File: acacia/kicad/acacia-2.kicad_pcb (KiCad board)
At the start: 2 copper layers, 274 x 158 mm, 127 parts, among them J1 USB4500-03-0-A, SW1 A, SW10 C, SW11 R, SW12 F, SW13 V, SW14 T, SW15 G, SW16 Back, SW17 Gui, SW18 Ctl, SW19 Alt, SW2 Z, SW20 Sft, SW21 Fwd, SW22 AltGr, SW23 L2, SW24 L1, SW25 Ctl, SW26 U, SW27 J, SW28 M, SW29 N, SW3 Tab, SW30 Enter, SW31 I, SW32 K, SW33 Comm, SW34 O, SW35 L, SW36 Dot, SW38 P, SW39 Semi, SW4 B, SW40 Slsh, SW41 H, SW42 Y, SW43 QMK, SW48 Q, SW49 RESET, SW5 W, SW6 S, SW7 X, SW8 E, SW9 D, U1 USBLC6-2SC6, U2 ATmega32U2-A, Y1 16MHz

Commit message: wip
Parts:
- removed D20, D25, D30, D41: D, Diode_SMD:D_0805_2012Metric_Pad1.15x1.40mm_HandSolder
- removed SW20: Sft, mech-kbd:MX-Hotswap-1U
- removed SW25: Ctl, mech-kbd:MX-Hotswap-1U
- removed SW29: N, mech-kbd:MX-Hotswap-1U
- removed SW30: Enter, mech-kbd:MX-Hotswap-1U
- removed SW43: QMK, Button_Switch_SMD:SW_SPST_EVQQ2
- removed TP5: C2, TestPoint:TestPoint_Pad_1.0x1.0mm
- removed TP6: C4, TestPoint:TestPoint_Pad_1.0x1.0mm
- removed TP7: C5, TestPoint:TestPoint_Pad_1.0x1.0mm
- added C10: 4µ7, Capacitor_SMD:CP_Elec_8x6.9, F.Cu at (110.4, 123.0)
- added C7: 47µ, Capacitor_SMD:CP_Elec_8x6.9, F.Cu at (110.4, 113.1)
- added C9: 100n, Capacitor_SMD:C_0805_2012Metric_Pad1.18x1.45mm_HandSolder, F.Cu at (95.3, 139.0)
- added FB3: 120@100M, Inductor_SMD:L_0805_2012Metric_Pad1.15x1.40mm_HandSolder, F.Cu at (90.6, 139.0)
- added FB4: 120@100M, Inductor_SMD:L_0805_2012Metric_Pad1.15x1.40mm_HandSolder, F.Cu at (90.6, 142.0)
- added U3: ATmega32U4-A, Package_QFP:TQFP-44_10x10mm_P0.8mm, F.Cu at (192.4, 123.8)
- D1, D10, D11, D12, D13, D14, D15, D16, D17, D18, D19, D2, D21, D22, D23, D24, D26, D27, D28, D29, D3, D31, D32, D33, D34, D35, D36, D37, D38, D39, D4, D40, D48, D5, D6, D7, D8, D9: moved to F.Cu
- SW12: value F -> T
- SW14: value T -> L1
- SW15: value G -> Prv
- SW16: value Back -> G
- SW17: value Gui -> B
- SW18: value Ctl -> Sft
- SW19: value Alt -> L2
- SW21: value Fwd -> H
- SW22: value AltGr -> K
- SW23: value L2 -> Spc
- SW24: value L1 -> Esc
- SW27: value J -> N
- SW32: value K -> E
- SW33: value Comm -> Com
- SW39: value Semi -> Y
- SW4: value B -> Nxt
- SW40: value Slsh -> J
- SW41: value H -> Del
- SW42: value Y -> Ent
- SW8: value E -> F
- TP1: value GND -> GNDD
- TP3: value D0 -> 5V; footprint TestPoint:TestPoint_Pad_1.0x1.0mm -> TestPoint:TestPoint_Pad_1.5x1.5mm; moved to F.Cu
- TP4: value D1 -> 3V3; footprint TestPoint:TestPoint_Pad_1.0x1.0mm -> TestPoint:TestPoint_Pad_1.5x1.5mm; moved to F.Cu
- U2: value ATmega32U2-A -> NCP1117; footprint Package_QFP:TQFP-32_7x7mm_P0.8mm -> Package_TO_SOT_SMD:TO-252-2; moved to F.Cu
- Y1: value 16MHz -> 8MHz
- moved SW21 217.2 mm to (37.7, 73.8), turned to 0 degrees
- moved SW42 205.3 mm to (78.1, 94.0), turned to 0 degrees
- moved SW40 199.0 mm to (78.1, 53.6), turned to 0 degrees
- moved SW36 194.7 mm to (57.9, 134.4), turned to 0 degrees
- moved SW39 194.6 mm to (78.1, 33.4), turned to 0 degrees
- moved H5 191.8 mm to (92.2, 119.7)
- moved SW38 190.6 mm to (78.1, 13.2), turned to 0 degrees
- moved SW22 188.3 mm to (37.7, 94.0), turned to 0 degrees
- moved SW35 187.8 mm to (57.9, 114.2), turned to 0 degrees
- moved SW28 181.0 mm to (57.9, 13.2), turned to 0 degrees
- moved SW34 181.0 mm to (57.9, 94.0), turned to 0 degrees
- moved SW27 173.3 mm to (37.7, 134.4), turned to 0 degrees
- moved SW33 170.6 mm to (57.9, 73.8), turned to 0 degrees
- moved SW26 164.8 mm to (37.7, 114.2), turned to 0 degrees
- moved SW32 163.5 mm to (57.9, 53.6), turned to 0 degrees
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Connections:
- C1 pad 1: GND -> GNDD
- C2 pad 1: Net-(C2-Pad1) -> GND
- C3 pad 1: Net-(C3-Pad1) -> Net-(U3-XTAL1)
- C3 pad 2: GND -> GNDD
- C4 pad 1: Net-(C4-Pad1) -> Net-(U3-XTAL2)
- C4 pad 2: GND -> GNDD
- C5 pad 1: Net-(C5-Pad1) -> Net-(U3-UCAP)
- C5 pad 2: GND -> GNDD
- C6 pad 2: GND -> GNDD
- C8 pad 1: +5V -> +3V3
- C8 pad 2: GND -> GNDD
- D15 pad 1: R4 -> R3
- D4 pad 1: R4 -> R3
- F1 pad 1: Net-(C1-Pad2) -> /VBUS
- F1 pad 2: +5V -> Net-(C1-Pad2)
- FB1 pad 1: GND -> GNDD
- FB1 pad 2: Net-(C2-Pad1) -> GND
- FB2 pad 1: /VBUS -> Net-(C1-Pad2)
- FB2 pad 2: Net-(C1-Pad2) -> +5V
- R1 pad 1: Net-(C2-Pad1) -> GND
- R4 pad 1: +5V -> +3V3
- R4 pad 2: Net-(C7-Pad1) -> Net-(R4-Pad2)
- R5 pad 1: Net-(C7-Pad1) -> Net-(R4-Pad2)
- R5 pad 2: ~{RESET} -> Net-(U3-~{RESET})
- R6 pad 1: Net-(R6-Pad1) -> Net-(U3-~{HWB}/PE2)
- R6 pad 2: GND -> GNDD
- SW15 pad 2: C3 -> C2
- SW4 pad 2: C0 -> C7
- SW49 pad 1: ~{RESET} -> Net-(R4-Pad2)
- SW49 pad 2: GND -> GNDD
- TP1 pad 1: GND -> GNDD
- TP3 pad 1: Net-(TP3-Pad1) -> Net-(C7-Pad1)
- TP4 pad 1: Net-(TP4-Pad1) -> +3V3
- U2 pad 1: Net-(C3-Pad1) -> GNDD
- U2 pad 2: Net-(C4-Pad1) -> +3V3
- U2 pad 3: GND -> +5V
- Y1 pad 1: Net-(C3-Pad1) -> Net-(U3-XTAL1)
- Y1 pad 2: Net-(C4-Pad1) -> Net-(U3-XTAL2)
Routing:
- net R4: track 382.6 -> 52.9 mm, vias 5 -> 0
- net R0: track 417.2 -> 107.1 mm, vias 10 -> 0
- net +3V3: track 0.00 -> 294.5 mm, vias 0 -> 1
- net (no net): track 0.00 -> 272.5 mm
- net R1: track 351.2 -> 595.2 mm, vias 13 -> 4
- net C0: track 217.2 -> 115.2 mm, vias 3 -> 1
- net C3: track 119.7 -> 45.2 mm, vias 3 -> 0
- net Net-(D26-A): track 4.04 -> 74.5 mm, vias 0 -> 2
- net Net-(D29-A): track 6.50 -> 71.5 mm
- net C7: track 162.9 -> 216.3 mm, vias 2 -> 0
- net C5: track 166.6 -> 215.2 mm
- net Net-(D20-Pad2): track 25.0 -> 0.00 mm
- net Net-(D22-A): track 10.8 -> 35.2 mm
- net GNDD: track 0.00 -> 17.8 mm, vias 0 -> 2
- net Net-(U3-XTAL1): track 0.00 -> 15.9 mm
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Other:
- board text added: "2023 jpsecher v2"
- board text removed: "2022 jpsecher"

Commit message: WIP: v2 board
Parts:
- removed C10: 4µ7, Capacitor_SMD:CP_Elec_8x6.9
- removed the C7 at (110.4, 113.1)
- removed the C7 at (144.5, 121.0)
- removed C9: 100n, Capacitor_SMD:C_0805_2012Metric_Pad1.18x1.45mm_HandSolder
- removed D48: D, Diode_SMD:D_0805_2012Metric_Pad1.15x1.40mm_HandSolder
- removed FB3, FB4: 120@100M, Inductor_SMD:L_0805_2012Metric_Pad1.15x1.40mm_HandSolder
- removed SW40: J, mech-kbd:MX-Hotswap-1U
- removed SW41: Del, mech-kbd:MX-Hotswap-1U
- removed SW42: Ent, mech-kbd:MX-Hotswap-1U
- removed SW48: Q, mech-kbd:MX-Hotswap-1U
- removed SW49: RESET, Button_Switch_SMD:SW_SPST_EVQQ2
- removed TP3: 5V, TestPoint:TestPoint_Pad_1.5x1.5mm
- removed TP4: 3V3, TestPoint:TestPoint_Pad_1.5x1.5mm
- removed U3: ATmega32U4-A, Package_QFP:TQFP-44_10x10mm_P0.8mm
- added C7: 4µ7, Capacitor_SMD:C_0805_2012Metric_Pad1.18x1.45mm_HandSolder, B.Cu at (125.8, 192.8)
- added D20: D, Diode_SMD:D_0805_2012Metric_Pad1.15x1.40mm_HandSolder, B.Cu at (116.2, 162.5)
- added D25: D, Diode_SMD:D_0805_2012Metric_Pad1.15x1.40mm_HandSolder, B.Cu at (111.4, 153.4)
- added D30: D, Diode_SMD:D_0805_2012Metric_Pad1.15x1.40mm_HandSolder, B.Cu at (111.4, 168.6)
- added D41: SK6805, LED_SMD:LED_SK6805_PLCC4_2.4x2.7mm_P1.3mm, B.Cu at (170.7, 146.6)
- added D42: SK6805, LED_SMD:LED_SK6805_PLCC4_2.4x2.7mm_P1.3mm, B.Cu at (177.9, 138.5)
- added D43: SK6805, LED_SMD:LED_SK6805_PLCC4_2.4x2.7mm_P1.3mm, B.Cu at (186.7, 138.6)
- added J2: USB4500-03-0-A, mech-kbd:USB4500030A, B.Cu at (158.9, 49.4)
- added SW20: Y, mech-kbd:MX-Hotswap-1U, F.Cu at (263.6, 67.8)
- added SW25: V, mech-kbd:MX-Hotswap-1U, F.Cu at (105.5, 90.2)
- added SW29: Com, mech-kbd:MX-Hotswap-1U, F.Cu at (226.1, 76.2)
- added SW30: Dot, mech-kbd:MX-Hotswap-1U, F.Cu at (247.0, 80.2)
- added SW37: Del, mech-kbd:MX-Hotswap-1U, F.Cu at (210.5, 111.1)
- C1: value 4µ7 -> 1µ; footprint Capacitor_SMD:C_0805_2012Metric_Pad1.18x1.45mm_HandSolder -> Capacitor_SMD:C_1206_3216Metric_Pad1.33x1.80mm_HandSolder
- C2: value 22p -> 1µ
- C6: footprint Capacitor_SMD:C_1206_3216Metric_Pad1.33x1.80mm_HandSolder -> Capacitor_SMD:C_0805_2012Metric_Pad1.18x1.45mm_HandSolder
- C8: value 1µ -> 22p
- D1, D10, D11, D12, D13, D14, D15, D16, D17, D18, D19, D2, D21, D22, D23, D24, D26, D27, D28, D29, D3, D31, D32, D33, D34, D35, D36, D37, D38, D4, D5, D6, D7, D8, D9, H1, H10, H2, H3, H4, H5, H6, H7, H8, H9: moved to B.Cu
- D39, D40: value D -> SK6805; footprint Diode_SMD:D_0805_2012Metric_Pad1.15x1.40mm_HandSolder -> LED_SMD:LED_SK6805_PLCC4_2.4x2.7mm_P1.3mm; moved to B.Cu
- J1: value USB4500-03-0-A -> Trackpad; footprint mech-kbd:USB4500030A -> Connector:FanPinHeader_1x04_P2.54mm_Vertical
- R1: value 1M -> 10k
- R3: value 22 -> 10k
- R4: value 10k -> 5k1
- R5: value 22 -> 5k1
- R6: value 10k -> 22
- R7: value 5k1 -> 22
- R8: value 5k1 -> 1M
- SW1: value A -> Q
- SW10: value C -> P
- SW11: value R -> A
- SW12: value T -> S
- SW13: value V -> D
- SW14: value L1 -> T
- SW15: value Prv -> B
- SW16: value G -> K
- SW17: value B -> N
- SW18: value Sft -> E; footprint mech-kbd:MX-Hotswap-1.5U -> mech-kbd:MX-Hotswap-1U
- SW19: value L2 -> L; footprint mech-kbd:MX-Hotswap-1.25U -> mech-kbd:MX-Hotswap-1U
- SW2: value Z -> W
- SW21: value H -> RESET; footprint mech-kbd:MX-Hotswap-1U -> Button_Switch_SMD:SW_SPST_EVQQ2; moved to B.Cu
- SW22: value K -> Z
- SW23: value Spc -> X; footprint mech-kbd:MX-Hotswap-1.5U -> mech-kbd:MX-Hotswap-1U
- SW24: value Esc -> C; footprint mech-kbd:MX-Hotswap-1.25U -> mech-kbd:MX-Hotswap-1U
- SW26: value U -> Sft; footprint mech-kbd:MX-Hotswap-1U -> mech-kbd:MX-Hotswap-1.5U
- SW27: value N -> Spc; footprint mech-kbd:MX-Hotswap-1U -> mech-kbd:MX-Hotswap-1.5U
- SW3: value Tab -> F
- SW31: value I -> J
- SW32: value E -> Tab; footprint mech-kbd:MX-Hotswap-1U -> mech-kbd:MX-Hotswap-1.5U
- SW33: value Com -> Prv; footprint mech-kbd:MX-Hotswap-1U -> mech-kbd:MX-Hotswap-1.5U
- SW34: value O -> L1
- SW35: value L -> L2; footprint mech-kbd:MX-Hotswap-1U -> mech-kbd:MX-Hotswap-1.5U
- SW36: value Dot -> Esc; footprint mech-kbd:MX-Hotswap-1U -> mech-kbd:MX-Hotswap-1.5U
- SW38: value P -> Nxt; footprint mech-kbd:MX-Hotswap-1U -> mech-kbd:MX-Hotswap-1.5U
- SW39: value Y -> Ent; footprint mech-kbd:MX-Hotswap-1U -> mech-kbd:MX-Hotswap-1.5U
- SW4: value Nxt -> R
- SW5: value W -> G
- SW6: value S -> H
- SW7: value X -> U
- SW8: value F -> I
- SW9: value D -> O
- TP1: value GNDD -> 5V
- TP2: value 5V -> GNDD
- U1: value USBLC6-2SC6 -> ATmega32U4-A; footprint Package_TO_SOT_SMD:SOT-23-6 -> Package_QFP:TQFP-44_10x10mm_P0.8mm
- U2: value NCP1117 -> USBLC6-2SC6; footprint Package_TO_SOT_SMD:TO-252-2 -> Package_TO_SOT_SMD:SOT-23-6; moved to B.Cu
- Y1: value 8MHz -> 16MHz
- moved SW10 241.1 mm to (258.6, 49.5), turned to 15 degrees
- moved SW9 219.9 mm to (237.2, 43.4), turned to 15 degrees
- moved SW7 217.9 mm to (199.6, 53.5), turned to 15 degrees
- moved SW31 217.1 mm to (268.5, 86.2), turned to 15 degrees
- moved SW39 206.0 mm to (282.0, 62.9), turned to -75 degrees
- moved SW8 200.4 mm to (216.2, 39.5), turned to 15 degrees
- moved SW6 192.3 mm to (183.9, 67.6), turned to 15 degrees
- moved H1 184.0 mm to (272.5, 51.1), turned to 180 degrees
- moved SW38 176.5 mm to (232.2, 99.2), turned to -75 degrees
- moved SW28 170.0 mm to (209.5, 90.1), turned to 15 degrees
- moved SW17 167.9 mm to (204.6, 71.8), turned to 15 degrees
- moved SW16 159.9 mm to (188.7, 86.0), turned to 15 degrees
- moved H2 158.4 mm to (250.5, 92.2), turned to 180 degrees
- moved SW27 155.3 mm to (191.9, 116.2), turned to -75 degrees
- moved H3 152.6 mm to (227.5, 33.2), turned to 180 degrees
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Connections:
- C1 pad 1: GNDD -> +5V
- C1 pad 2: Net-(C1-Pad2) -> GNDD
- C2 pad 1: GND -> +5V
- C2 pad 2: GNDPWR -> GNDD
- C3 pad 1: Net-(U3-XTAL1) -> Net-(U1-XTAL1)
- C4 pad 1: Net-(U3-XTAL2) -> Net-(U1-XTAL2)
- C5 pad 1: Net-(U3-UCAP) -> Net-(U1-UCAP)
- C8 pad 1: +3V3 -> GND
- C8 pad 2: GNDD -> GNDPWR
- D1 pad 1: R1 -> R0
- D10 pad 1: R2 -> R0
- D11 pad 1: R0 -> R1
- D13 pad 1: R2 -> R1
- D14 pad 1: R3 -> R1
- D15 pad 1: R3 -> R1
- D16 pad 1: R0 -> R1
- D18 pad 1: R2 -> R1
- D19 pad 1: R3 -> R1
- D2 pad 1: R2 -> R0
- D21 pad 1: R0 -> R2
- D22 pad 1: R1 -> R2
- D24 pad 1: R3 -> R2
- D26 pad 1: R0 -> R2
- D27 pad 1: R1 -> R2
- D29 pad 1: R3 -> R2
- D3 pad 1: R3 -> R0
- D31 pad 1: R0 -> R3
- D32 pad 1: R1 -> R3
- D33 pad 1: R2 -> R3
- D34 pad 1: R0 -> R3
- D35 pad 1: R1 -> R3
- D36 pad 1: R2 -> R3
- D37 pad 1: R0 -> R3
- D38 pad 1: R1 -> R3
- D39 pad 1: R2 -> Net-(D39-DOUT)
- D39 pad 2: Net-(D39-A) -> GNDD
- D4 pad 1: R3 -> R0
- D40 pad 1: R3 -> Net-(D40-DOUT)
- D40 pad 2: Net-(D40-A) -> GNDD
- D6 pad 1: R1 -> R0
- D7 pad 1: R2 -> R0
- D9 pad 1: R1 -> R0
- F1 pad 2: Net-(C1-Pad2) -> Net-(C7-Pad2)
- FB1 pad 1: GNDD -> Net-(C7-Pad2)
- FB1 pad 2: GND -> +5V
- FB2 pad 1: Net-(C1-Pad2) -> GNDD
- FB2 pad 2: +5V -> GND
- R1 pad 1: GND -> +5V
- R1 pad 2: GNDPWR -> Net-(R1-Pad2)
- R2 pad 1: /DDD- -> Net-(R1-Pad2)
- R2 pad 2: DDDD- -> Net-(U1-~{RESET})
- R3 pad 1: /DDD+ -> Net-(U1-~{HWB}/PE2)
- R3 pad 2: DDDD+ -> GNDD
- R4 pad 1: +3V3 -> Net-(J2-CC1)
- R4 pad 2: Net-(R4-Pad2) -> GND
- R5 pad 1: Net-(R4-Pad2) -> Net-(J2-CC2)
- R5 pad 2: Net-(U3-~{RESET}) -> GND
- R6 pad 1: Net-(U3-~{HWB}/PE2) -> /DDD-
- R6 pad 2: GNDD -> DDDD-
- R7 pad 1: Net-(J1-CC1) -> /DDD+
- R7 pad 2: GND -> DDDD+
- R8 pad 1: Net-(J1-CC2) -> GND
- R8 pad 2: GND -> GNDPWR
- SW10 pad 2: C2 -> C9
- SW11 pad 2: C3 -> C0
- SW12 pad 2: C3 -> C1
- SW13 pad 2: C3 -> C2
- SW15 pad 2: C2 -> C4
- SW16 pad 2: C4 -> C5
- SW17 pad 2: C4 -> C6
- SW18 pad 2: C4 -> C7
- SW19 pad 2: C4 -> C8
- SW2 pad 2: C0 -> C1
- SW21 pad 1: Net-(D21-A) -> Net-(R1-Pad2)
- SW21 pad 2: C5 -> GNDD
- SW22 pad 1: Net-(D22-A) -> Net-(D21-A)
- SW22 pad 2: C5 -> C0
- SW23 pad 1: Net-(D23-A) -> Net-(D22-A)
- SW23 pad 2: C5 -> C1
- SW24 pad 1: Net-(D24-A) -> Net-(D23-A)
- SW24 pad 2: C5 -> C2
- SW26 pad 1: Net-(D26-A) -> Net-(D25-A)
- SW26 pad 2: C6 -> C4
- SW27 pad 1: Net-(D27-A) -> Net-(D26-A)
- SW27 pad 2: C6 -> C5
- SW28 pad 1: Net-(D28-A) -> Net-(D27-A)
- SW3 pad 2: C0 -> C2
- SW31 pad 1: Net-(D31-A) -> Net-(D30-A)
- SW31 pad 2: C7 -> C9
- SW32 pad 1: Net-(D32-A) -> Net-(D31-A)
- SW32 pad 2: C7 -> C0
- SW33 pad 1: Net-(D33-A) -> Net-(D32-A)
- SW33 pad 2: C7 -> C2
- SW34 pad 1: Net-(D34-A) -> Net-(D33-A)
- SW34 pad 2: C8 -> C3
- SW35 pad 1: Net-(D35-A) -> Net-(D34-A)
- SW35 pad 2: C8 -> C4
- SW36 pad 1: Net-(D36-A) -> Net-(D35-A)
- SW36 pad 2: C8 -> C5
- SW38 pad 2: C9 -> C7
- SW4 pad 2: C7 -> C3
- SW5 pad 2: C1 -> C4
- SW6 pad 2: C1 -> C5
- SW7 pad 2: C1 -> C6
- SW8 pad 2: C2 -> C7
- SW9 pad 2: C2 -> C8
- TP1 pad 1: GNDD -> +5V
- TP2 pad 1: +5V -> GNDD
- U1 pad 1: /D+ -> unconnected-(U1-PE6-Pad1)
- U1 pad 2: GNDPWR -> +5V
- U1 pad 3: /D- -> DDDD-
- U1 pad 4: /DD- -> DDDD+
- U1 pad 5: /VBUS -> GNDD
- U1 pad 6: /DD+ -> Net-(U1-UCAP)
- U2 pad 1: GNDD -> /D+
- U2 pad 2: +3V3 -> GNDPWR
- U2 pad 3: +5V -> /D-
- Y1 pad 1: Net-(U3-XTAL1) -> Net-(U1-XTAL1)
- Y1 pad 2: Net-(U3-XTAL2) -> Net-(U1-XTAL2)
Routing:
- net R1: track 595.2 -> 0.00 mm, vias 4 -> 0
- net R3: track 423.0 -> 0.00 mm, vias 2 -> 0
- net R2: track 320.2 -> 0.00 mm, vias 3 -> 0
- net +3V3: track 294.5 -> 0.00 mm, vias 1 -> 0
- net (no net): track 272.5 -> 0.00 mm
- net C9: track 235.5 -> 0.00 mm, vias 1 -> 0
- net C7: track 216.3 -> 0.00 mm
- net C5: track 215.2 -> 0.00 mm
- net C4: track 184.4 -> 0.00 mm
- net C8: track 182.1 -> 0.00 mm, vias 2 -> 0
- net C6: track 156.9 -> 0.00 mm, vias 1 -> 0
- net C1: track 138.7 -> 0.00 mm, vias 1 -> 0
- net C2: track 123.1 -> 0.00 mm, vias 1 -> 0
- net C0: track 115.2 -> 0.00 mm, vias 1 -> 0
- net +5V: track 108.5 -> 0.00 mm, vias 2 -> 0
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- removed copper zone on B.Cu, net GND
- removed copper zone on F.Cu, net GND
- removed copper zone on F.Cu, net GNDPWR
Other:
- board size 274 x 158 mm -> 268 x 112 mm

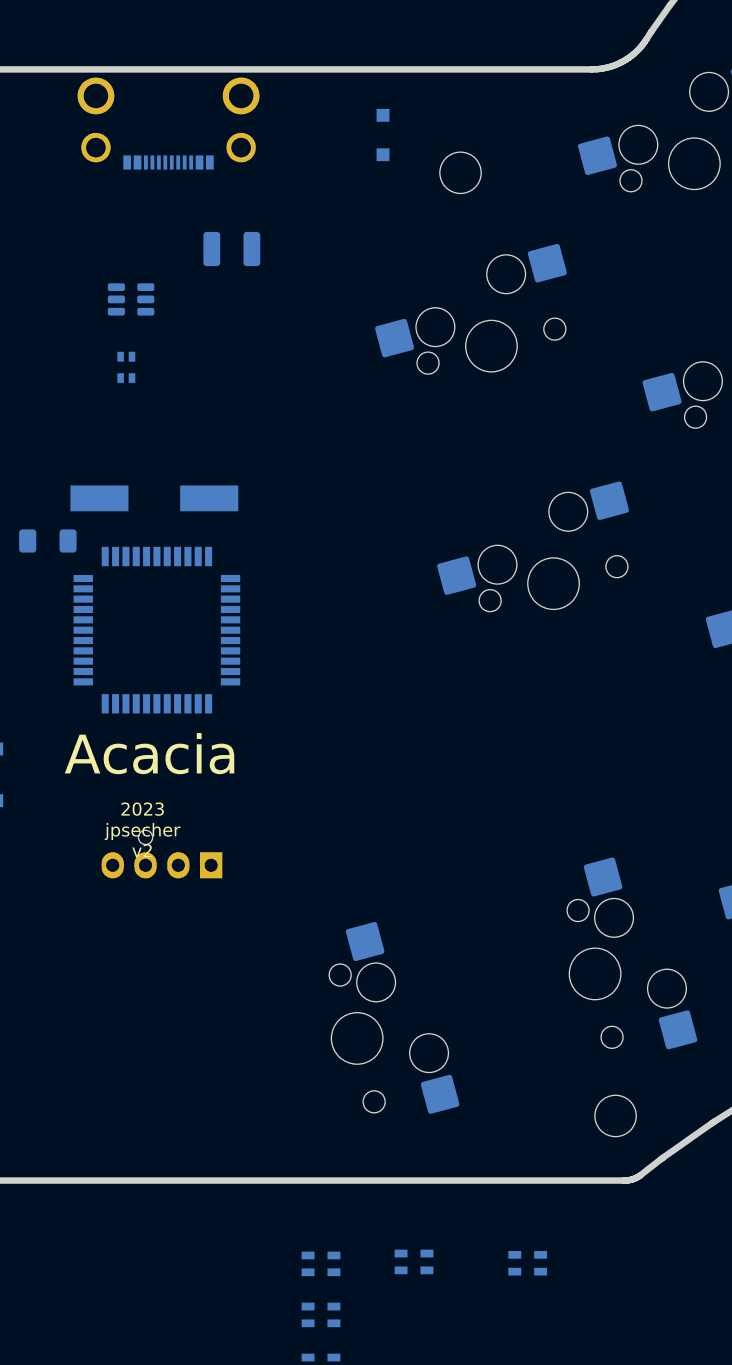
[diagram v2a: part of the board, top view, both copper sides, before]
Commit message: New USB connector
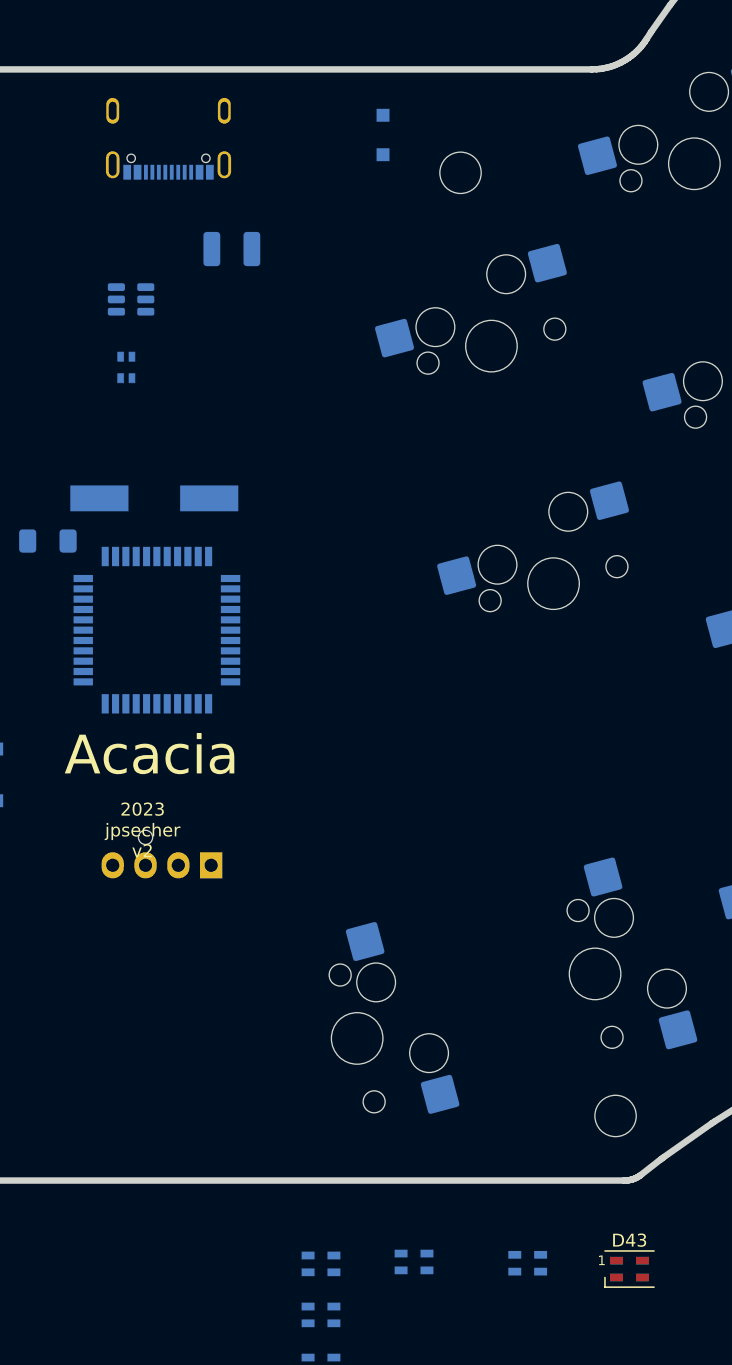
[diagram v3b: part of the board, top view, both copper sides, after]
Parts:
- added D43: SK6805, LED_SMD:LED_SK6805_PLCC4_2.4x2.7mm_P1.3mm, F.Cu at (194.6, 139.1)
- J2: value USB4500-03-0-A -> USB4105-GF-A-060; footprint mech-kbd:USB4500030A -> mech-kbd:GCT_USB4105-GF-A
- renumbered D43 to D44
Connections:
- D44 pad 3: Net-(D42-DOUT) -> Net-(D43-DOUT)

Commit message: WIP
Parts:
- added J3: USB4105-GF-A-060, mech-kbd:GCT_USB4105-GF-A, B.Cu at (157.6, 49.3)
- added R3: 22, Resistor_SMD:R_0805_2012Metric_Pad1.20x1.40mm_HandSolder, B.Cu at (169.0, 90.0)
- added R4: 22, Resistor_SMD:R_0805_2012Metric_Pad1.20x1.40mm_HandSolder, B.Cu at (167.0, 90.0)
- D39, D40, D41, D42, D44: moved to F.Cu
- F1: footprint Resistor_SMD:R_1210_3225Metric_Pad1.30x2.65mm_HandSolder -> Resistor_SMD:R_1206_3216Metric_Pad1.30x1.75mm_HandSolder
- J1: value Trackpad -> GroveMiniTrack; footprint Connector:FanPinHeader_1x04_P2.54mm_Vertical -> Connector_JST:JST_XA_B04B-XASK-1-A_1x04_P2.50mm_Vertical; moved to F.Cu
- J2: value USB4105-GF-A-060 -> TM040040; footprint mech-kbd:GCT_USB4105-GF-A -> Connector_FFC-FPC:Hirose_FH12-12S-0.5SH_1x12-1MP_P0.50mm_Horizontal
- SW14: value T -> F
- SW15: value B -> G
- SW16: value K -> H
- SW17: value N -> J
- SW18: value E -> K
- SW20: value Y -> B
- SW28: value M -> N
- SW29: value Com -> M
- SW3: value F -> E
- SW30: value Dot -> Com
- SW31: value J -> Dot
- SW35: value L2 -> AGr
- SW5: value G -> T
- SW6: value H -> Y
- TP1, TP2: footprint TestPoint:TestPoint_Pad_1.0x1.0mm -> TestPoint:TestPoint_Pad_D1.5mm
- moved D38 201.8 mm to (277.0, 60.5)
- moved D30 172.5 mm to (265.5, 91.0)
- moved D20 169.2 mm to (259.5, 72.5)
- moved D10 168.6 mm to (255.0, 54.0)
- moved D8 157.3 mm to (214.0, 44.5)
- moved D9 155.2 mm to (235.0, 48.0)
- moved D19 153.5 mm to (238.0, 66.0)
- moved D29 153.3 mm to (241.5, 84.5)
- moved C8 148.8 mm to (166.0, 52.5)
- moved R10 147.5 mm to (166.0, 49.5)
- moved R6 143.8 mm to (147.0, 52.0), turned to -90 degrees
- moved D37 138.5 mm to (227.0, 97.0)
- moved D28 137.8 mm to (222.5, 81.0)
- moved D18 137.4 mm to (217.0, 63.0)
- moved C7 134.7 mm to (162.0, 63.0), turned to 0 degrees
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- renumbered R8 to R10, R3 to R5, R4 to R6, R5 to R7, R6 to R8, R7 to R9
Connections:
- FL1 pad 1: /DDD+ -> /DDD-
- FL1 pad 2: /DD+ -> /DD-
- FL1 pad 3: /DD- -> /DD+
- FL1 pad 4: /DDD- -> /DDD+
- J1 pad 1: +5V -> GNDD
- J1 pad 2: /SCL -> +5V
- J1 pad 3: /SDA -> /SCL
- J1 pad 4: GNDD -> /SCL
- R6 pad 1: Net-(J2-CC1) -> Net-(J3-CC1)
- R7 pad 1: Net-(J2-CC2) -> Net-(J3-CC2)
- R8 pad 1: /DDD- -> /DDD+
- R8 pad 2: DDDD- -> DDDD+
- R9 pad 1: /DDD+ -> /DDD-
- R9 pad 2: DDDD+ -> DDDD-
- U1 pad 1: unconnected-(U1-PE6-Pad1) -> /BTN
- U1 pad 18: /SCL -> Net-(U1-PD0)
- U1 pad 19: /SDA -> Net-(U1-PD1)
- U2 pad 1: /D+ -> /D-
- U2 pad 3: /D- -> /D+
- U2 pad 4: /DD- -> /DD+
- U2 pad 6: /DD+ -> /DD-
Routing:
- net C0: track 0.00 -> 185.9 mm, vias 0 -> 2
- net R0: track 0.00 -> 167.5 mm, vias 0 -> 9
- net R3: track 0.00 -> 150.2 mm, vias 0 -> 3
- net C1: track 0.00 -> 150.2 mm, vias 0 -> 4
- net C2: track 0.00 -> 145.6 mm, vias 0 -> 4
- net R2: track 0.00 -> 143.6 mm, vias 0 -> 6
- net R1: track 0.00 -> 135.7 mm, vias 0 -> 7
- net C5: track 0.00 -> 85.7 mm
- net C7: track 0.00 -> 78.8 mm
- net C4: track 0.00 -> 73.4 mm
- net +5V: track 0.00 -> 70.1 mm, vias 0 -> 2
- net C6: track 0.00 -> 63.0 mm
- net C3: track 0.00 -> 62.1 mm
- net C8: track 0.00 -> 40.8 mm
- net C9: track 0.00 -> 40.8 mm
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- added copper zone on B.Cu, net GNDD
- added copper zone on F.Cu, net GNDD
- added copper zone on B.Cu, net GNDPWR

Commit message: before reordering
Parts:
- moved D16 13.2 mm to (180.0, 79.0), turned to -90 degrees
- moved D17 12.8 mm to (195.0, 66.5), turned to -90 degrees
- moved D36 12.1 mm to (201.0, 105.0), turned to -90 degrees
- moved D6 11.5 mm to (174.5, 62.5), turned to -90 degrees
- moved D26 11.1 mm to (195.5, 105.0), turned to -90 degrees
- moved D35 11.0 mm to (174.0, 108.0), turned to -90 degrees
- moved C6 10.5 mm to (184.5, 112.0)
- moved D30 10.1 mm to (256.5, 86.5), turned to 0 degrees
- moved D38 9.24 mm to (279.0, 69.5), turned to 90 degrees
- moved D9 9.16 mm to (226.5, 44.5), turned to 90 degrees
- moved D7 8.91 mm to (188.5, 54.5), turned to 90 degrees
- moved D8 5.61 mm to (208.5, 43.5), turned to 90 degrees
- moved D10 5.22 mm to (250.0, 52.5), turned to 0 degrees
- moved D18 4.92 mm to (212.5, 61.0), turned to 0 degrees
- moved D20 4.79 mm to (255.0, 71.0), turned to 0 degrees
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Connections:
- U1 pad 1: /BTN -> unconnected-(U1-PE6-Pad1)
- U1 pad 28: unconnected-(U1-PB4-Pad28) -> /BTN
- U1 pad 29: unconnected-(U1-PB5-Pad29) -> RGB
- U1 pad 8: RGB -> unconnected-(U1-PB0-Pad8)
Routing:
- net R3: track 150.2 -> 340.5 mm, vias 3 -> 6
- net C9: track 40.8 -> 201.7 mm, vias 0 -> 2
- net R2: track 143.6 -> 301.2 mm, vias 6 -> 11
- net R1: track 135.7 -> 273.5 mm, vias 7 -> 15
- net R0: track 167.5 -> 302.4 mm, vias 9 -> 15
- net C8: track 40.8 -> 168.6 mm, vias 0 -> 2
- net C7: track 78.8 -> 160.8 mm, vias 0 -> 2
- net C5: track 85.7 -> 149.2 mm, vias 0 -> 2
- net C6: track 63.0 -> 122.5 mm, vias 0 -> 2
- net C3: track 62.1 -> 119.4 mm, vias 0 -> 4
- net C4: track 73.4 -> 102.9 mm, vias 0 -> 2
- net Net-(U1-~{RESET}): track 0.00 -> 23.9 mm, vias 0 -> 2
- net Net-(D38-A): track 0.00 -> 15.4 mm
- net Net-(D37-A): track 0.00 -> 7.43 mm
- net Net-(D16-A): track 0.00 -> 5.88 mm
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
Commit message: leds
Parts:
- added C9: 1µ, Capacitor_SMD:C_0805_2012Metric_Pad1.18x1.45mm_HandSolder, B.Cu at (150.5, 85.0)
- moved C6 44.1 mm to (140.5, 110.0)
- moved J2 3.75 mm to (157.8, 99.6)
- moved TP1 3.64 mm to (165.0, 65.5)
- moved TP2 3.61 mm to (165.0, 68.5)
- moved C7 3.14 mm to (165.0, 62.0), turned to -90 degrees
- moved R5 3.00 mm to (153.5, 89.0), turned to 180 degrees
- moved D9 2.04 mm to (227.0, 46.5)
- moved FB1 2.00 mm to (168.0, 64.0)
- moved R3 1.58 mm to (167.5, 90.5)
- moved R4 1.58 mm to (165.5, 90.5)
- moved D39 1.52 mm to (103.0, 115.5), turned to -15 degrees
- moved D41 1.52 mm to (146.0, 122.5), turned to 75 degrees
- moved D42 1.52 mm to (169.0, 122.5), turned to -75 degrees
- moved D40 1.19 mm to (127.5, 117.5), turned to 75 degrees
- moved D43 1.19 mm to (187.0, 117.5), turned to -75 degrees
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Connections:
- J1 pad 3: /SCL -> /SDA
- U1 pad 20: C2 -> C5
- U1 pad 21: C1 -> C8
- U1 pad 22: R0 -> C9
- U1 pad 25: C0 -> R3
- U1 pad 28: /BTN -> R2
- U1 pad 30: unconnected-(U1-PB6-Pad30) -> /BTN
- U1 pad 31: C4 -> unconnected-(U1-PC6-Pad31)
- U1 pad 32: C3 -> C4
- U1 pad 36: R3 -> C3
- U1 pad 37: R2 -> C0
- U1 pad 38: R1 -> C2
- U1 pad 39: C5 -> C1
- U1 pad 40: C8 -> R0
- U1 pad 41: C9 -> R1
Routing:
- net +5V: track 70.1 -> 276.6 mm, vias 2 -> 8
- net GNDD: track 6.87 -> 185.9 mm, vias 0 -> 12
- net RGB: track 0.00 -> 77.5 mm, vias 0 -> 3
- net Net-(D39-DOUT): track 0.00 -> 29.4 mm
- net /SDA: track 0.00 -> 29.2 mm
- net /SCL: track 0.00 -> 28.5 mm
- net Net-(D43-DOUT): track 0.00 -> 27.8 mm
- net C8: track 168.6 -> 143.4 mm
- net Net-(D41-DOUT): track 0.00 -> 24.9 mm
- net Net-(D40-DOUT): track 0.00 -> 24.4 mm
- net C9: track 201.7 -> 178.1 mm
- net Net-(D42-DOUT): track 0.00 -> 20.2 mm
- net R1: track 273.5 -> 292.4 mm, vias 15 -> 14
- net R0: track 302.4 -> 283.6 mm, vias 15 -> 13
- net /BTN: track 0.00 -> 15.6 mm, vias 0 -> 2
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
